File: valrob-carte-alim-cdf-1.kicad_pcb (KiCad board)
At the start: 4 copper layers, 194 parts, among them J1 USB_C_Receptacle_USB2.0_14P, J10 Conn_01x02, J11 Conn_01x02, J12 Conn_01x02, J13 Conn_01x02, J14 Conn_01x02, J15 Conn_01x02, J16 Conn_01x02, J17 Conn_01x02, J18 Conn_01x02, J19 Conn_01x02, J2 Conn_01x02, J20 Conn_01x02, J21 Conn_01x02, J22 Conn_01x02, J3 Conn_01x04_Pin, J4 Conn_01x02, J5 Conn_01x02, J6 Conn_01x02, J7 Conn_01x02, J8 Conn_01x02, J9 Conn_01x02, SW1 SW_Push, SW2 SW_Push, SW3 SW_Push, U1 SN65HVD230, U10 TPS259472A, U11 TPS259472A, U12 TPS259472A, U2 ESP32-S3-WROOM-1, U3 TLV75733PDBV, U4 TPS56A37, U5 TPS56A37, U6 TPS259472A, U7 TPS259472A, U8 TPS259472A, U9 TPS259472A

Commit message: pcb: add initial rough layout
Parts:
- SW2, SW3: footprint Connector_JST:JST_XH_B2B-XH-A_1x02_P2.50mm_Vertical -> Button_Switch_SMD:SW_SPST_TS-1088-xR020
- moved C36 270.0 mm to (204.6, 130.5)
- moved C37 270.0 mm to (204.6, 132.4)
- moved C38 270.0 mm to (204.6, 134.4)
- moved U9 270.0 mm to (205.6, 137.6)
- moved R44 268.9 mm to (201.7, 132.5)
- moved R45 268.9 mm to (201.7, 134.5)
- moved R47 268.9 mm to (201.7, 138.4)
- moved R48 268.9 mm to (201.7, 140.4)
- moved R50 268.9 mm to (201.7, 144.4)
- moved R43 268.9 mm to (201.7, 130.5)
- moved R46 268.9 mm to (201.7, 136.5)
- moved R49 268.9 mm to (201.7, 142.4)
- moved D16 264.8 mm to (205.4, 141.2)
- moved JP6 262.8 mm to (202.6, 147.7)
- moved C9 240.5 mm to (121.5, 73.0)
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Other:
- board outline added: 94.5 x 58.5 mm

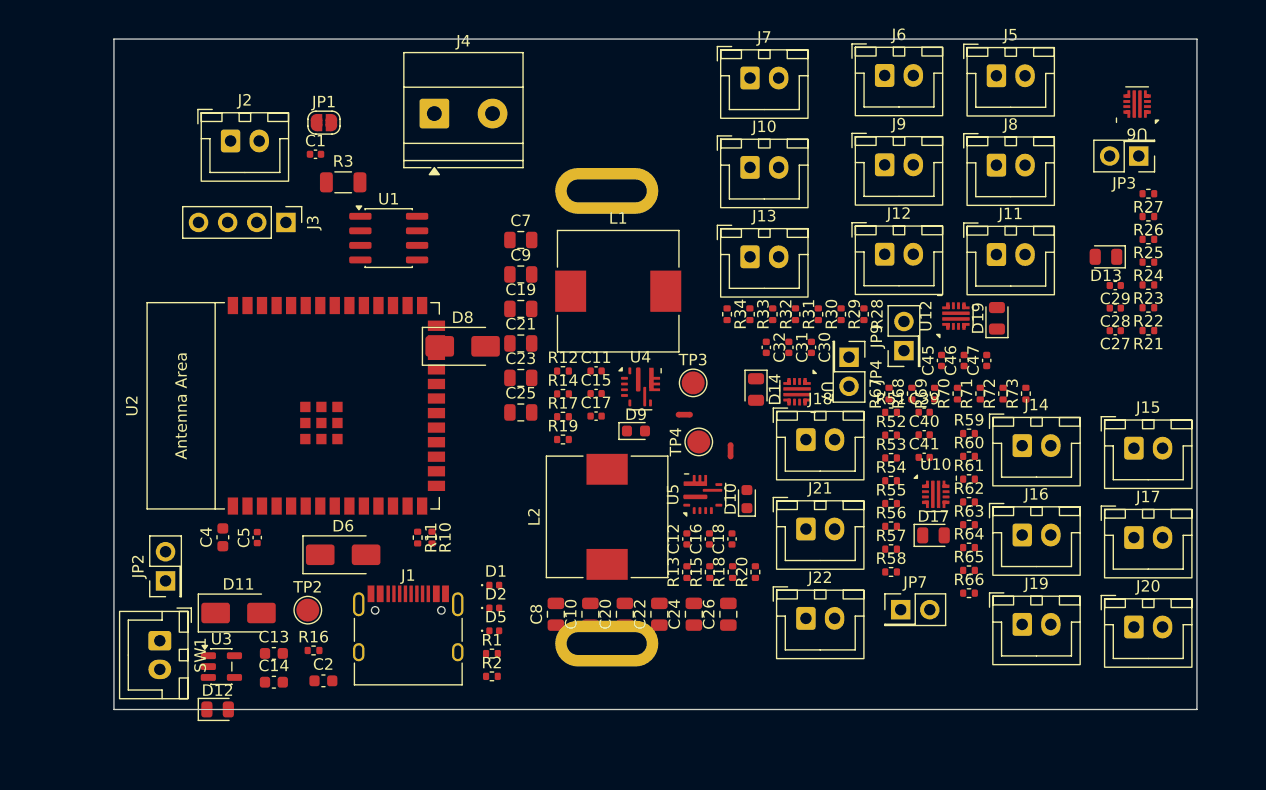
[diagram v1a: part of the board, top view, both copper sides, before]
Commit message: pcb: refine layout
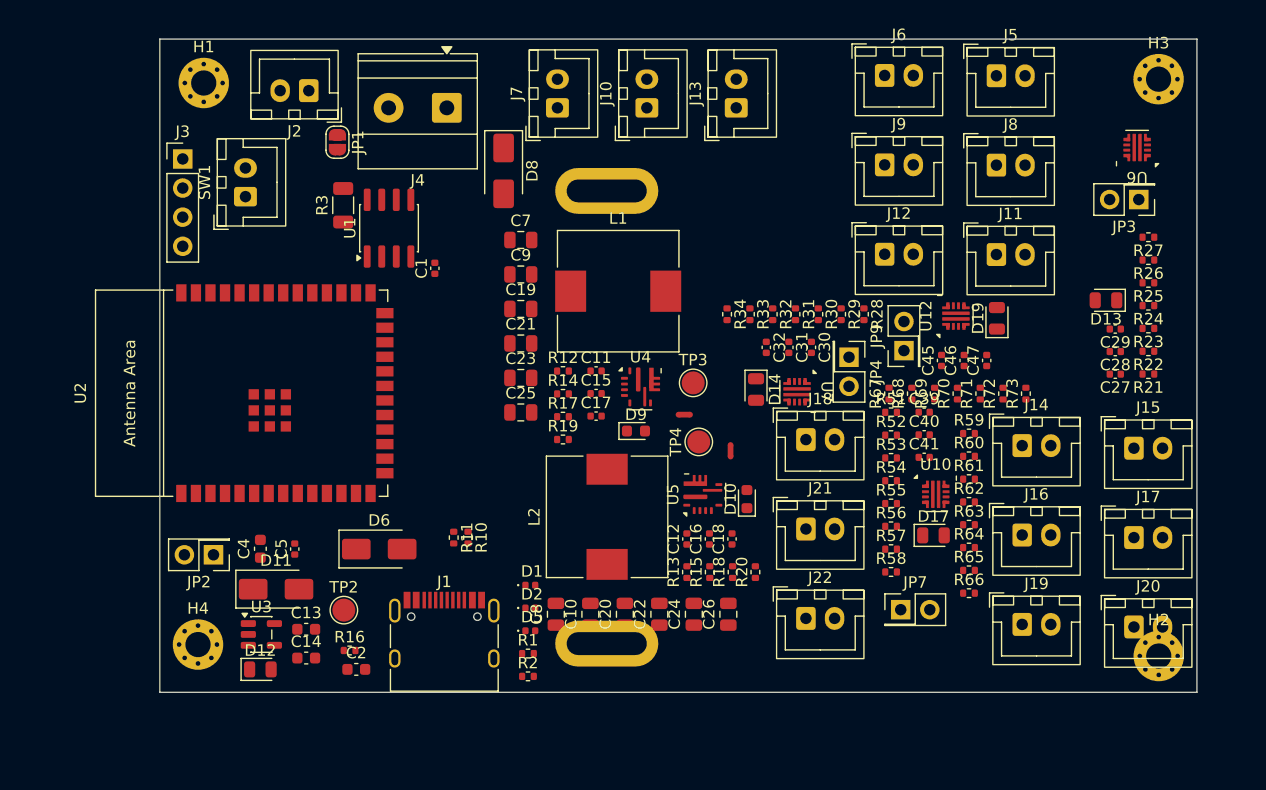
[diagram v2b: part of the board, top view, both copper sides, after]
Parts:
- added H1: MountingHole_Pad, MountingHole:MountingHole_2.2mm_M2_Pad_Via, F.Cu at (93.8, 56.3)
- added H2: MountingHole_Pad, MountingHole:MountingHole_2.2mm_M2_Pad_Via, F.Cu at (177.2, 106.3)
- added H3: MountingHole_Pad, MountingHole:MountingHole_2.2mm_M2_Pad_Via, F.Cu at (177.2, 56.0)
- added H4: MountingHole_Pad, MountingHole:MountingHole_2.2mm_M2_Pad_Via, F.Cu at (93.3, 105.3)
- moved SW1 39.5 mm to (97.5, 66.2), turned to 90 degrees
- moved J7 17.0 mm to (124.7, 58.5), turned to 90 degrees
- moved D8 15.7 mm to (120.0, 64.0), turned to -90 degrees
- moved C1 14.4 mm to (114.0, 72.5), turned to 90 degrees
- moved J13 13.1 mm to (140.3, 58.5), turned to 90 degrees
- moved J3 10.6 mm to (92.0, 63.0), turned to 0 degrees
- moved J10 10.4 mm to (132.5, 58.5), turned to 90 degrees
- moved J2 8.11 mm to (103.0, 57.0), turned to 180 degrees
- moved D12 5.11 mm to (98.8, 107.5)
- moved JP2 4.76 mm to (94.7, 97.5), turned to 180 degrees
- moved U2 4.63 mm to (100.1, 83.4)
- moved U3 4.48 mm to (98.9, 104.5)
- moved D11 3.88 mm to (100.1, 100.5)
- moved C27 3.80 mm to (173.4, 81.7)
- moved C28 3.80 mm to (173.4, 79.8)
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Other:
- board size 94.5 x 58.5 mm -> 90.5 x 57 mm

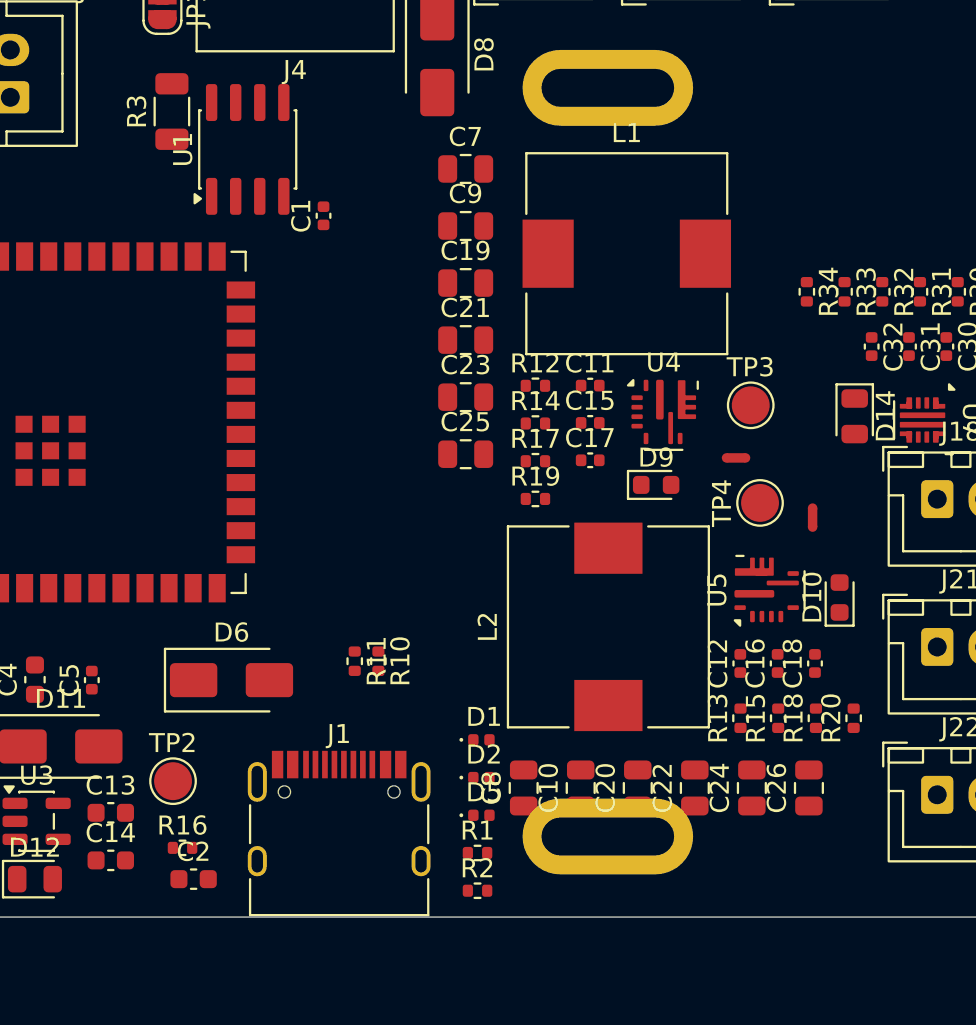
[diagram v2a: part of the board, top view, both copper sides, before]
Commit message: pcb: add smps layout
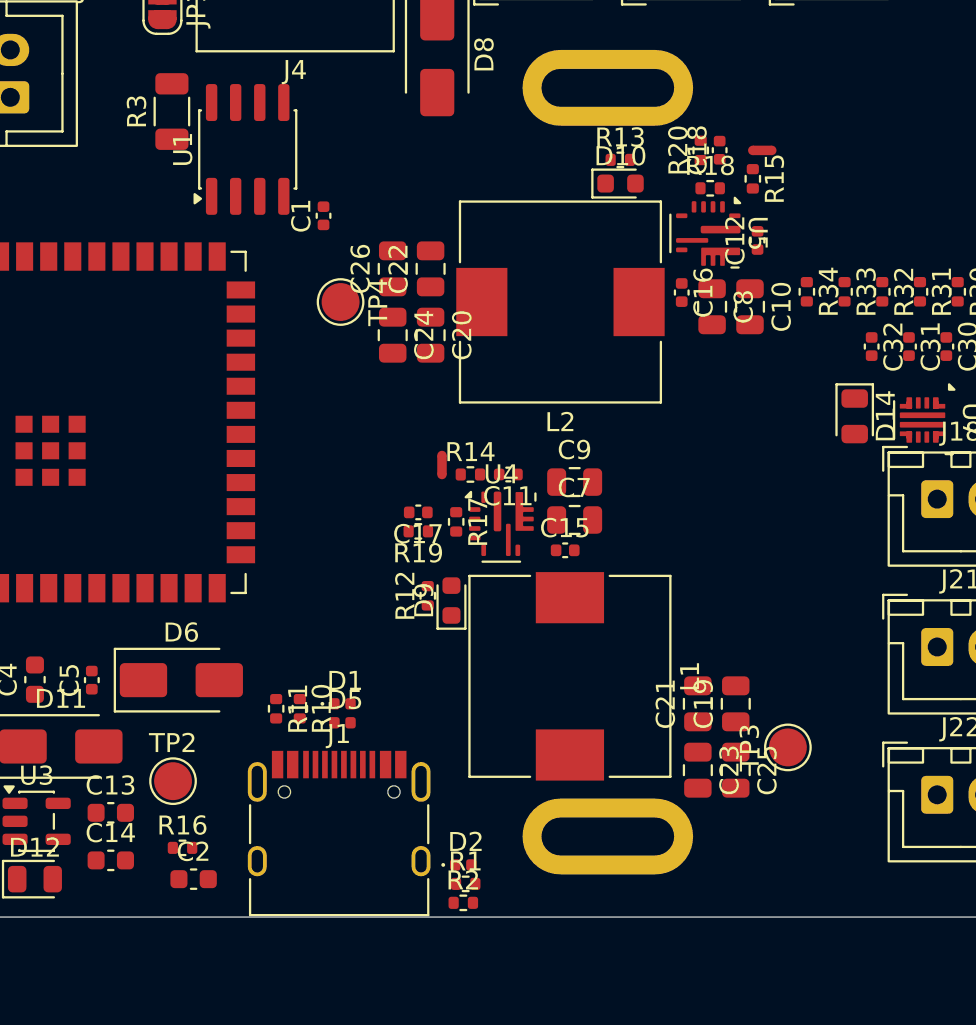
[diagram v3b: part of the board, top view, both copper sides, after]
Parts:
- moved C26 35.1 mm to (117.7, 75.3)
- moved R20 31.0 mm to (133.9, 69.0)
- moved C22 30.7 mm to (119.7, 75.3)
- moved C24 30.5 mm to (117.7, 78.8), turned to -90 degrees
- moved R13 30.1 mm to (129.7, 69.5), turned to 0 degrees
- moved R18 28.5 mm to (134.4, 71.0), turned to 0 degrees
- moved R15 28.5 mm to (136.7, 70.5), turned to -90 degrees
- moved C18 27.5 mm to (134.9, 69.0)
- moved C8 27.3 mm to (134.5, 77.3), turned to -90 degrees
- moved C10 26.9 mm to (136.5, 77.3), turned to -90 degrees
- moved C19 26.4 mm to (135.8, 98.2), turned to 90 degrees
- moved C20 26.3 mm to (119.7, 78.8), turned to -90 degrees
- moved D10 24.7 mm to (129.7, 70.8), turned to 0 degrees
- moved TP4 24.5 mm to (114.9, 77.0), turned to -90 degrees
- moved C23 23.2 mm to (133.8, 101.8), turned to -90 degrees
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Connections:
- R12 pad 1: +12V -> +3V3
- R13 pad 1: +12V -> +3V3

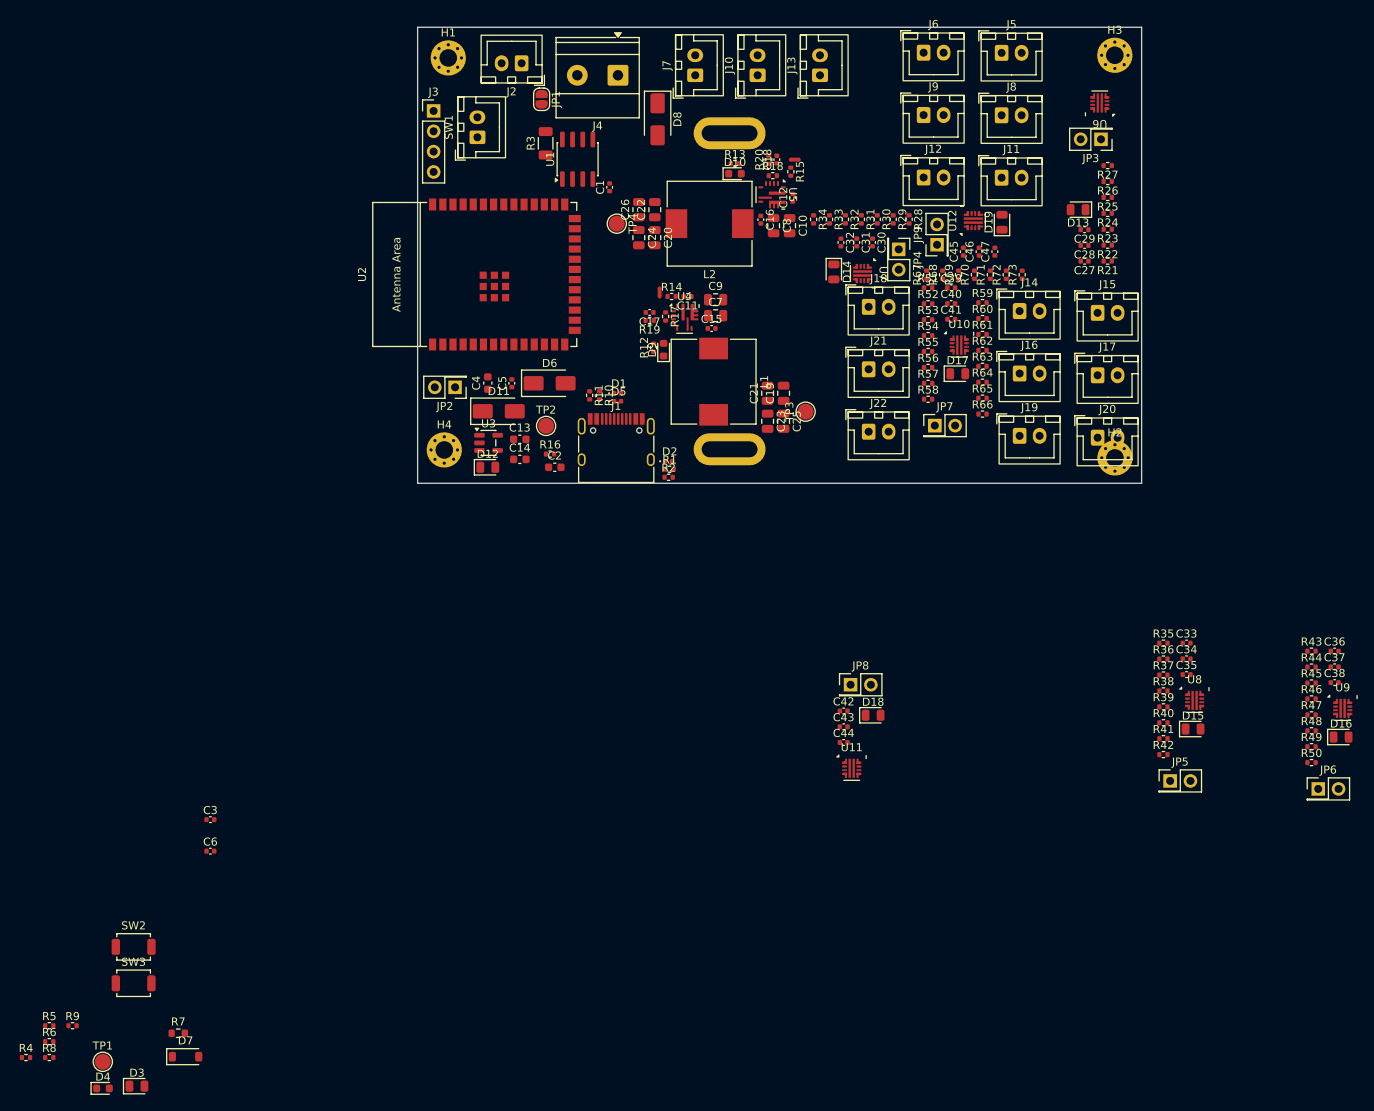
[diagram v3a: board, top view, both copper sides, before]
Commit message: pcb: add efuse layout
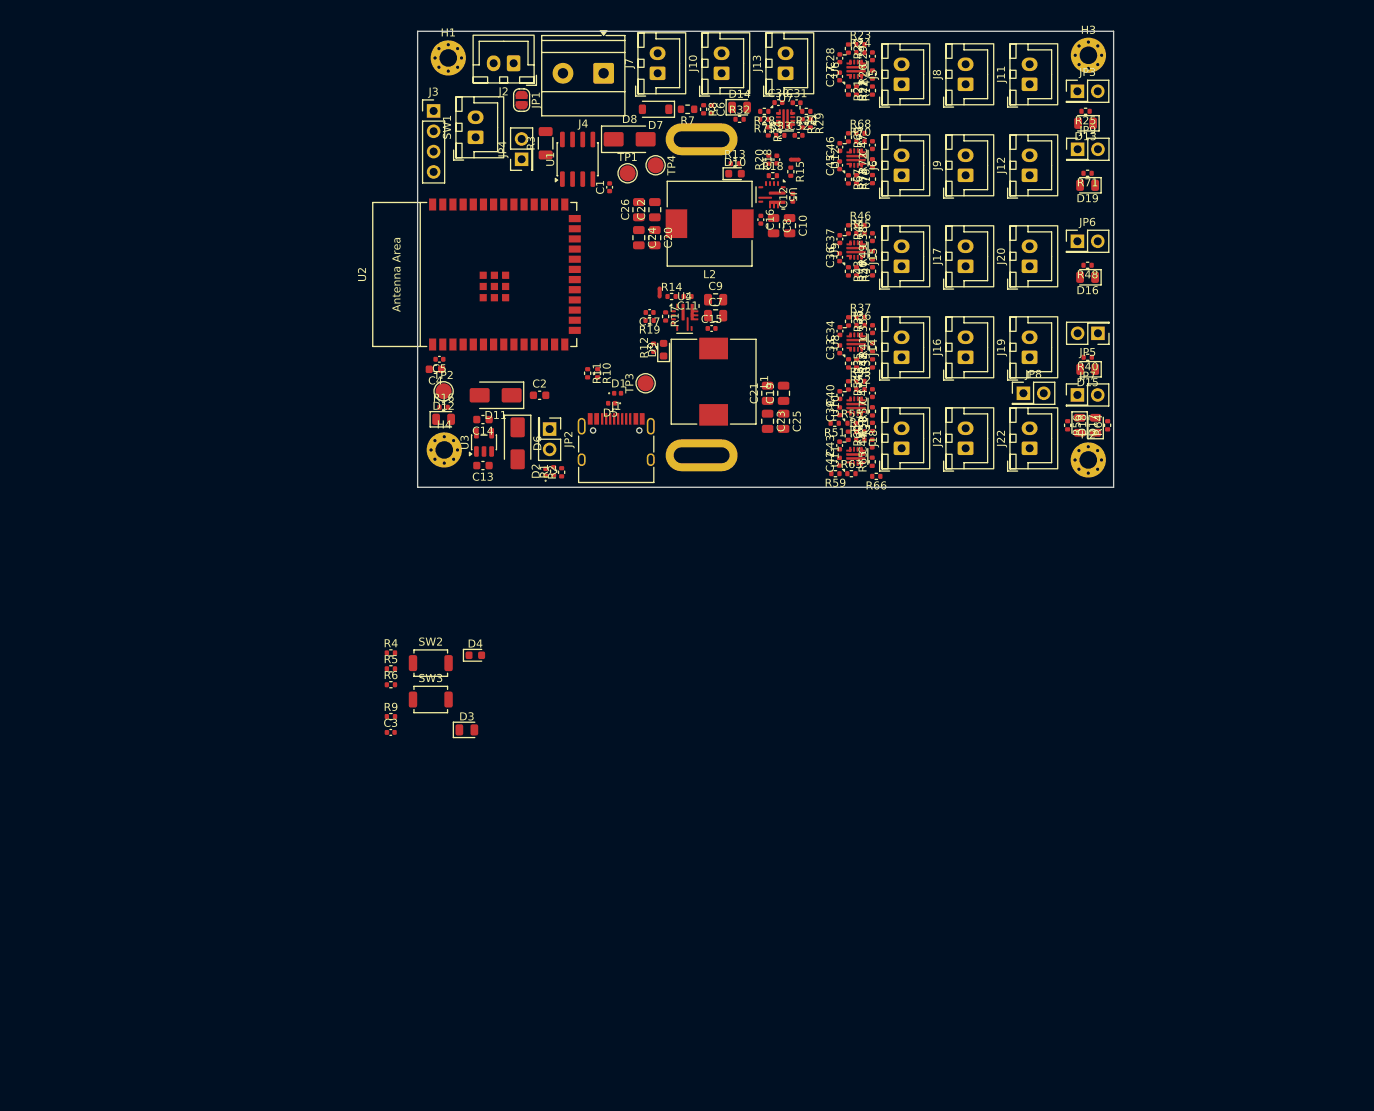
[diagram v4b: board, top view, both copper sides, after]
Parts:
- added R74: R, Resistor_SMD:R_0402_1005Metric, F.Cu at (144.8, 60.4)
- added R75: R, Resistor_SMD:R_0402_1005Metric, F.Cu at (133.3, 64.0)
- added R76: R, Resistor_SMD:R_0402_1005Metric, F.Cu at (144.8, 71.5)
- moved R8 144.0 mm to (125.8, 62.8), turned to -90 degrees
- moved D7 132.2 mm to (119.8, 62.8), turned to 180 degrees
- moved R7 131.9 mm to (123.8, 62.8), turned to 180 degrees
- moved TP1 129.0 mm to (116.2, 70.8)
- moved C6 111.9 mm to (126.8, 62.8), turned to -90 degrees
- moved U9 83.6 mm to (144.8, 80.3), turned to 90 degrees
- moved R49 82.4 mm to (146.8, 81.0), turned to 90 degrees
- moved R50 82.4 mm to (146.9, 83.0), turned to 90 degrees
- moved C37 81.8 mm to (142.8, 79.0), turned to 90 degrees
- moved R46 81.8 mm to (145.3, 77.3)
- moved C38 80.2 mm to (146.8, 78.7), turned to 90 degrees
- moved R44 79.7 mm to (143.8, 77.8), turned to -90 degrees
- moved R45 79.6 mm to (145.3, 78.3)
- moved R47 79.4 mm to (144.8, 83.0), turned to -90 degrees
- moved C36 79.1 mm to (142.8, 81.2), turned to 90 degrees
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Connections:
- U12 pad 2: unconnected-(U12-OVCSEL-Pad2) -> Net-(U12-OVCSEL)
- U6 pad 2: unconnected-(U6-OVCSEL-Pad2) -> Net-(U6-OVCSEL)
- U7 pad 2: unconnected-(U7-OVCSEL-Pad2) -> Net-(U7-OVCSEL)
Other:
- board size 90.5 x 57 mm -> 87 x 57 mm
